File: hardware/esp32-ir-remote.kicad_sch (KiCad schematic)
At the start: 52 parts, among them J2 USB_C_Receptacle_USB2.0_14P, J4 GPIO_PWR, J5 EXT_IR, Q3 AO3400A, SW1 RESET, SW2 BOOT, U1 AP63203WU, U3 ESP32-WROOM-32E, U4 TSOP382xx, U5 AM2302

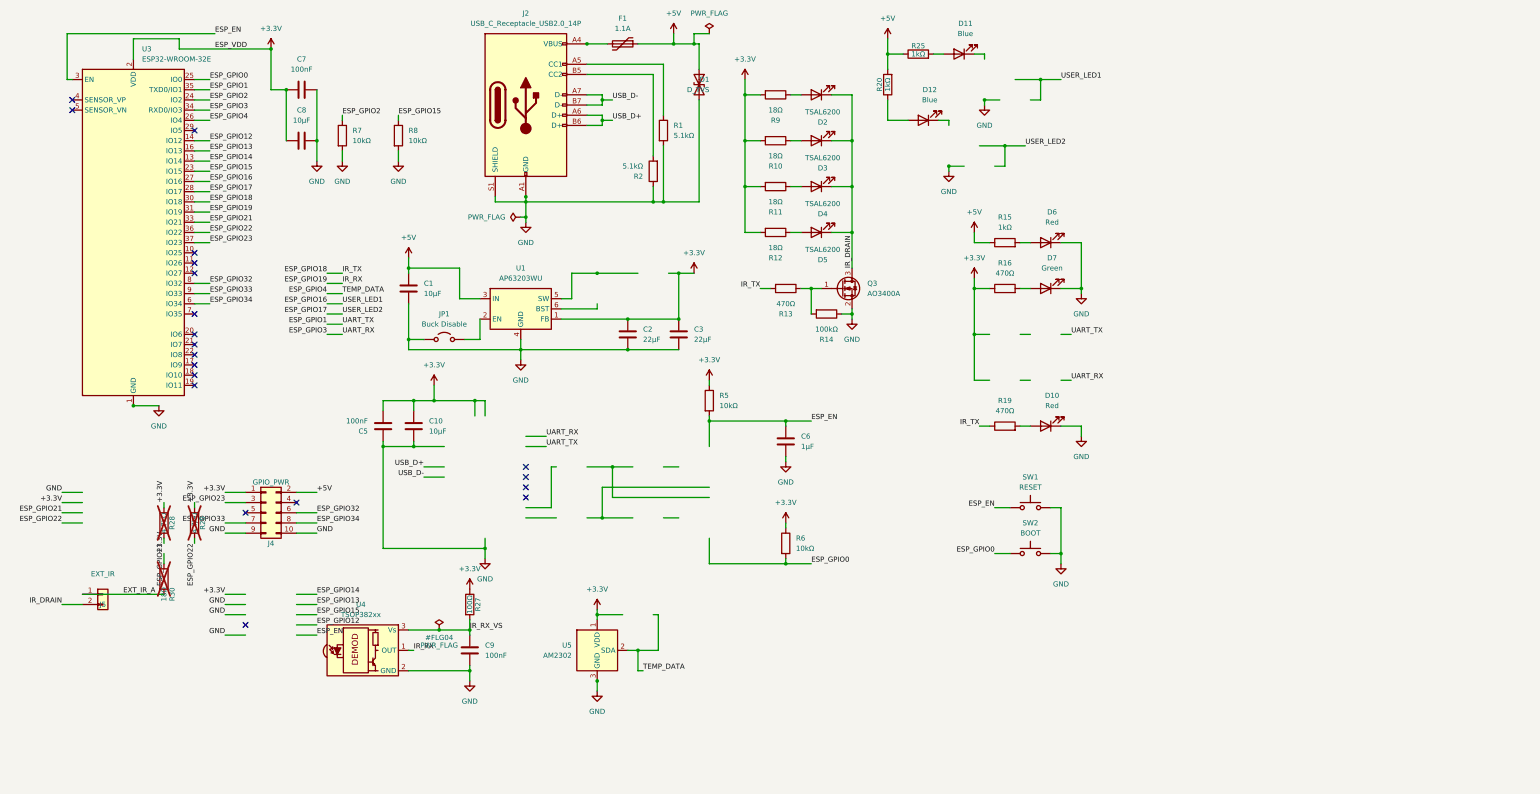
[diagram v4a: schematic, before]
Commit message: wip(sch): board v2 rewire complete — GOLDEN OK (all 36 nets match)
Swapped U1->AMS1117, U3->ESP32-C3, U5->AHT20 (delete+re-add); re-added the
5 movers (R7/R8 strap pull-ups, R20/R25 user-LED resistors, JP1) to break
their old power-rail ties; wired ~50 connections via connect_to_net. Verified
against scripts/ci/golden_netlist_v2.py: every intended v2 net (C3 pinout,
AMS1117 LDO + JP1 disconnect, AHT20 I2C bus, native USB D±, strapping
pull-ups, direct-GPIO user LEDs, repurposed J4 spare header) matches exactly.
Still TODO: 0805/colour LED footprints, 22ohm, un-DNP R28/R29, SMD USB-C,
orphan-wire cleanup, ERC.
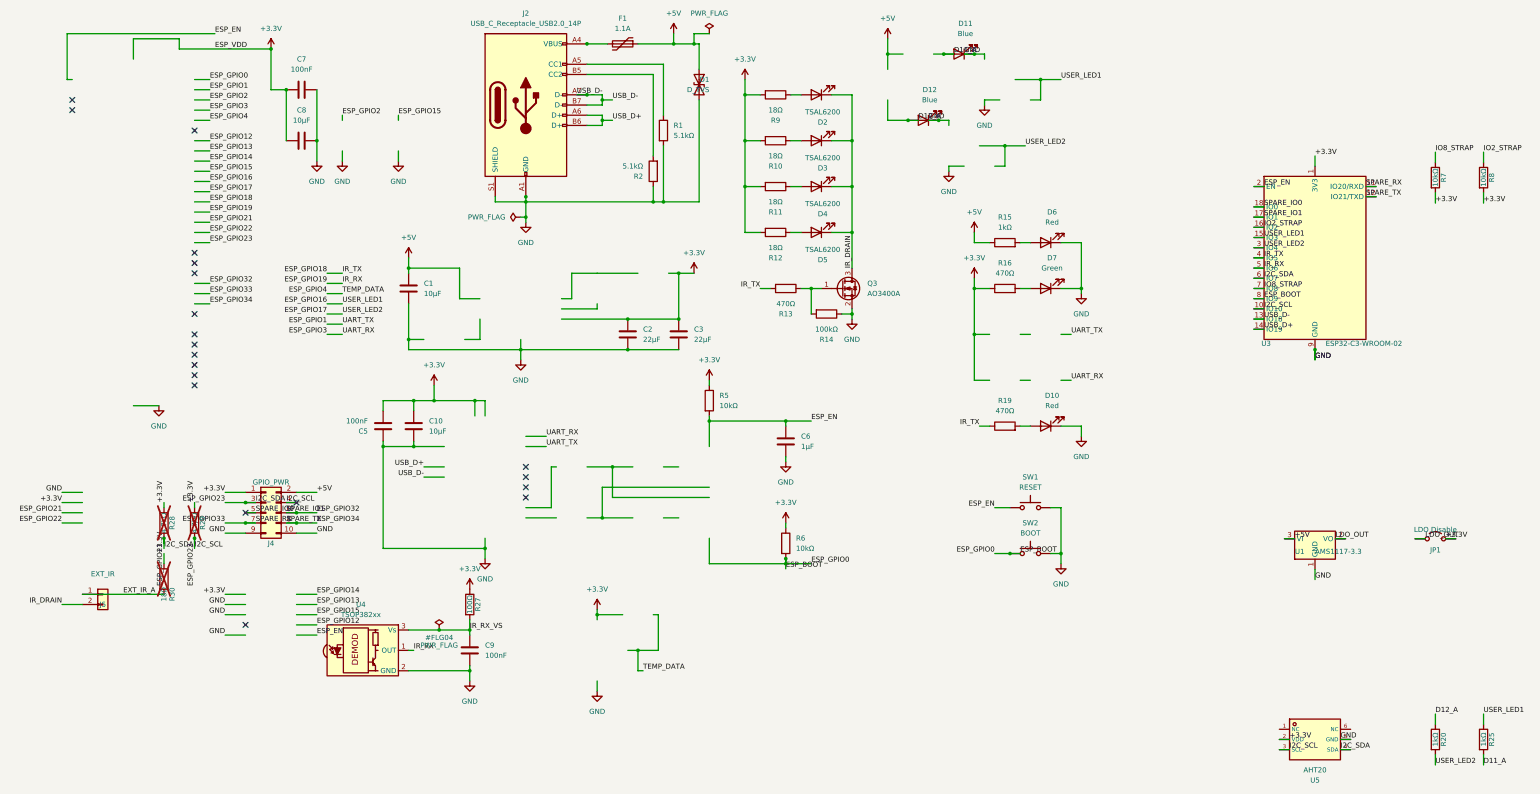
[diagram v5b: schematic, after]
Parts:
- removed U1: AP63203WU, Package_TO_SOT_SMD:TSOT-23-6, symbol Regulator_Switching:AP63203WU
- removed U3: ESP32-WROOM-32E, RF_Module:ESP32-WROOM-32D, symbol RF_Module:ESP32-WROOM-32E
- removed U5: AM2302, Sensor:ASAIR_AM2302_P2.54mm_Vertical, symbol Sensor:AM2302
- added U1: AMS1117-3.3, Package_TO_SOT_SMD:SOT-223-3_TabPin2, symbol Regulator_Linear:AMS1117-3.3
- added U3: ESP32-C3-WROOM-02, RF_Module:ESP32-C3-WROOM-02, symbol RF_Module:ESP32-C3-WROOM-02
- added U5: AHT20, JLC-MCP:SENSOR-SMD_L3.0-W3.0-P1.00-BR, symbol JLC-MCP-Sensors:AHT20_C2757850
- JP1: value Buck Disable -> LDO Disable
- R20, R25: LCSC C17513 -> (none)
- R7, R8: value 10kΩ -> 10kΩ; LCSC C17902 -> (none)
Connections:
- net ESP_GPIO23 is gone; now on net ESP_GPIO21: J4.3 (Pin_3)
- net +3.3V: now also JP1.2 (B), R7.2, R8.2, U3.1 (3V3), U5.2 (VDD)
- net +5V: now also U1.3 (VI); no longer R20.2, R25.1
- net ESP_EN: now also U3.2 (EN)
- net ESP_GPIO15: no longer R8.1
- net ESP_GPIO16: now also R25.1, U3.15 (IO3)
- net ESP_GPIO17: now also R20.2, U3.3 (IO4)
- net ESP_GPIO18: now also U3.4 (IO5)
- net ESP_GPIO19: now also U3.5 (IO6)
- net ESP_GPIO2: no longer R7.1
- net ESP_GPIO21: now also U3.6 (IO7), U5.4 (SDA)
- net ESP_GPIO22: now also J4.4 (Pin_4), U3.10 (IO10), U5.3 (SCL)
- net ESP_GPIO32: now also U3.17 (IO1)
- net ESP_GPIO33: now also U3.11 (IO20/RXD)
- net ESP_GPIO34: now also U3.12 (IO21/TXD)
- net GND: now also D11.1 (K), D12.1 (K), U1.1 (GND), U3.19 (GND), U3.9 (GND), U5.5 (GND); no longer JP1.1 (A), R7.2, R8.2
- net USB_D+: now also U3.14 (IO19)
- net USB_D-: now also U3.13 (IO18)
- net D12_A: now reaches D12.2 (A), R20.1
- net D11_A: now reaches D11.2 (A), R25.2
- net SPARE_IO0: now reaches J4.5 (Pin_5)
- net SPARE_IO0: now also U3.18 (IO0)
- net ESP_GPIO0 renamed ESP_BOOT
- net ESP_BOOT: now also U3.8 (IO9)
- new net IO2_STRAP: R8.1, U3.16 (IO2)
- new net IO8_STRAP: R7.1, U3.7 (IO8)
- new net LDO_OUT: JP1.1 (A), U1.2 (VO)

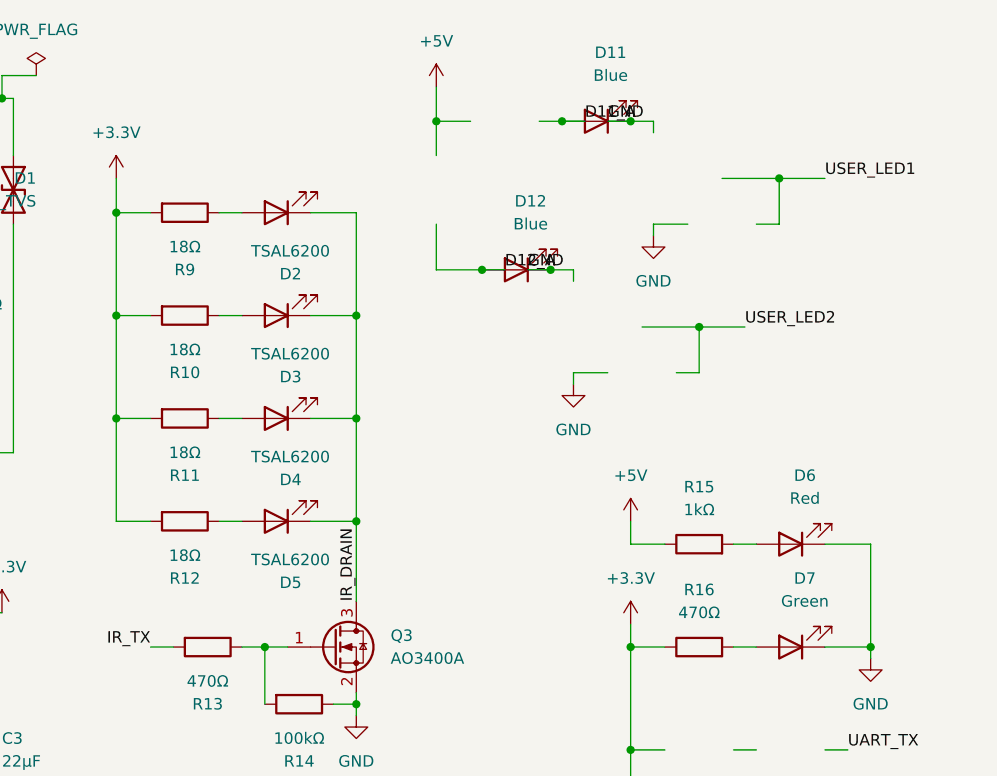
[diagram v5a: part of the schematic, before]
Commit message: wip(sch): v2 BOM attrs — 0805 LEDs (red system/yellow user), 22ohm IR, LCSC
D6/D7/D10 red + D11/D12 yellow 0805 (LED_SMD), R9-12 -> 22ohm (C17958),
LCSC on all new/re-added parts (C3 C2934560, AMS1117 C6186, AHT20 C2757850,
strap/user-LED resistors). GOLDEN OK still holds (attrs don't change nets).
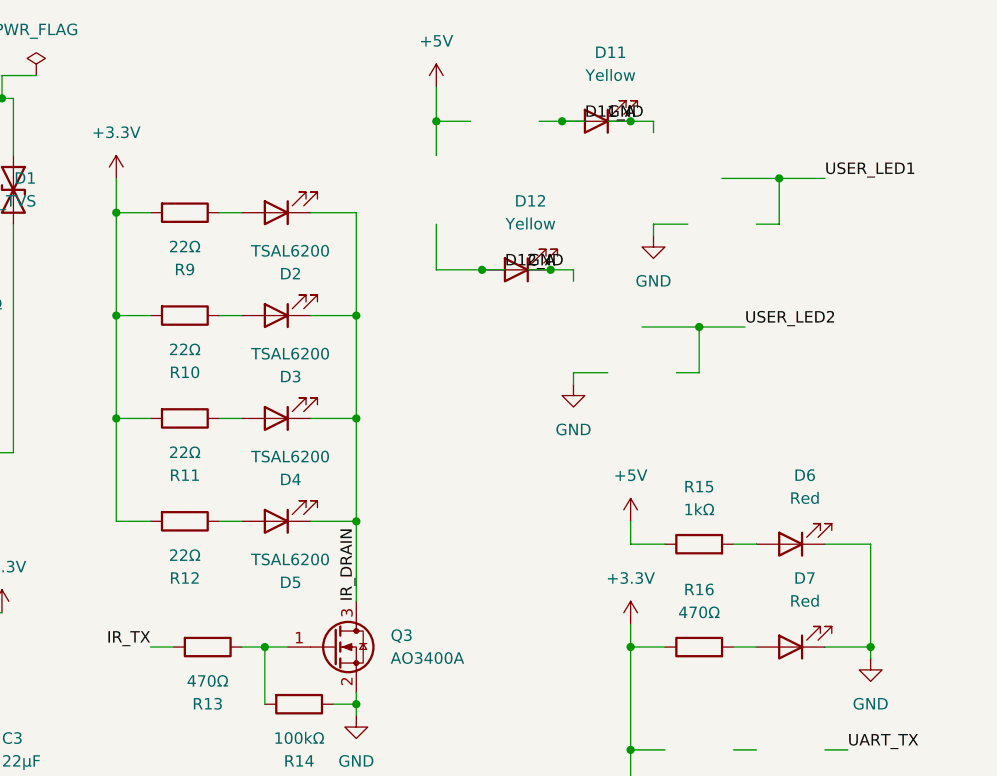
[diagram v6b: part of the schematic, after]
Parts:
- D10, D6: footprint LED_THT:LED_D3.0mm -> LED_SMD:LED_0805_2012Metric; LCSC C99772 -> C84256
- D11, D12: value Blue -> Yellow; footprint LED_THT:LED_D3.0mm -> LED_SMD:LED_0805_2012Metric; LCSC C86881 -> C2296
- D7: value Green -> Red; footprint LED_THT:LED_D3.0mm -> LED_SMD:LED_0805_2012Metric; LCSC C85161 -> C84256
- R10, R11, R12, R9: value 18Ω -> 22Ω; LCSC C17922 -> C17958
- R20, R25: LCSC (none) -> C17513
- R7, R8: LCSC (none) -> C17902
- U1: LCSC (none) -> C6186
- U3: LCSC (none) -> C2934560
- U5: LCSC (none) -> C2757850
